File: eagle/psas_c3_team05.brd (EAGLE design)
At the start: 100 x 71.2 mm, 92 parts, among them IC1 CP2102, J1 3220-10-0100-00, U1 MIC5319 3.3V, U2 MCP73871, X1 32 MHz

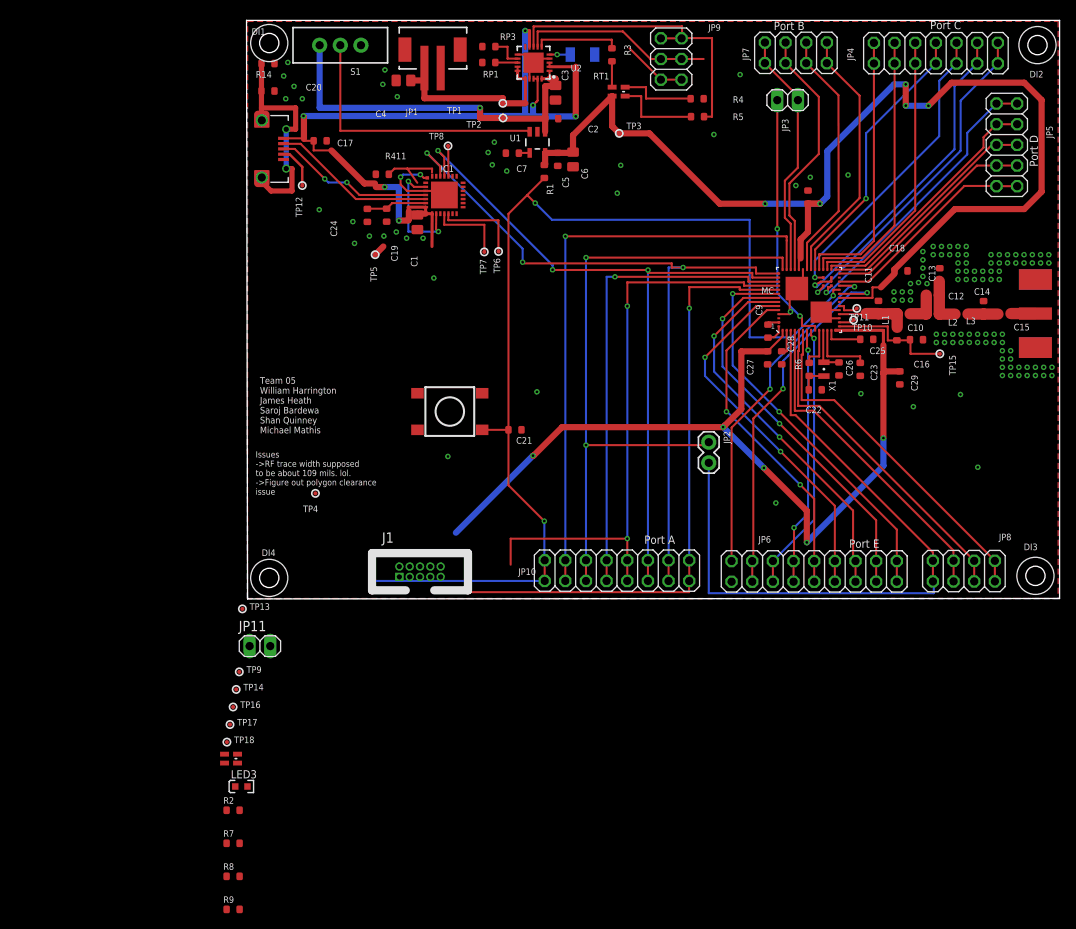
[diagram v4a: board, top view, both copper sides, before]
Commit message: major board cleanup and shrinkage. OOPS: just found out the uC pinout is wrong. Committing before doing that change.
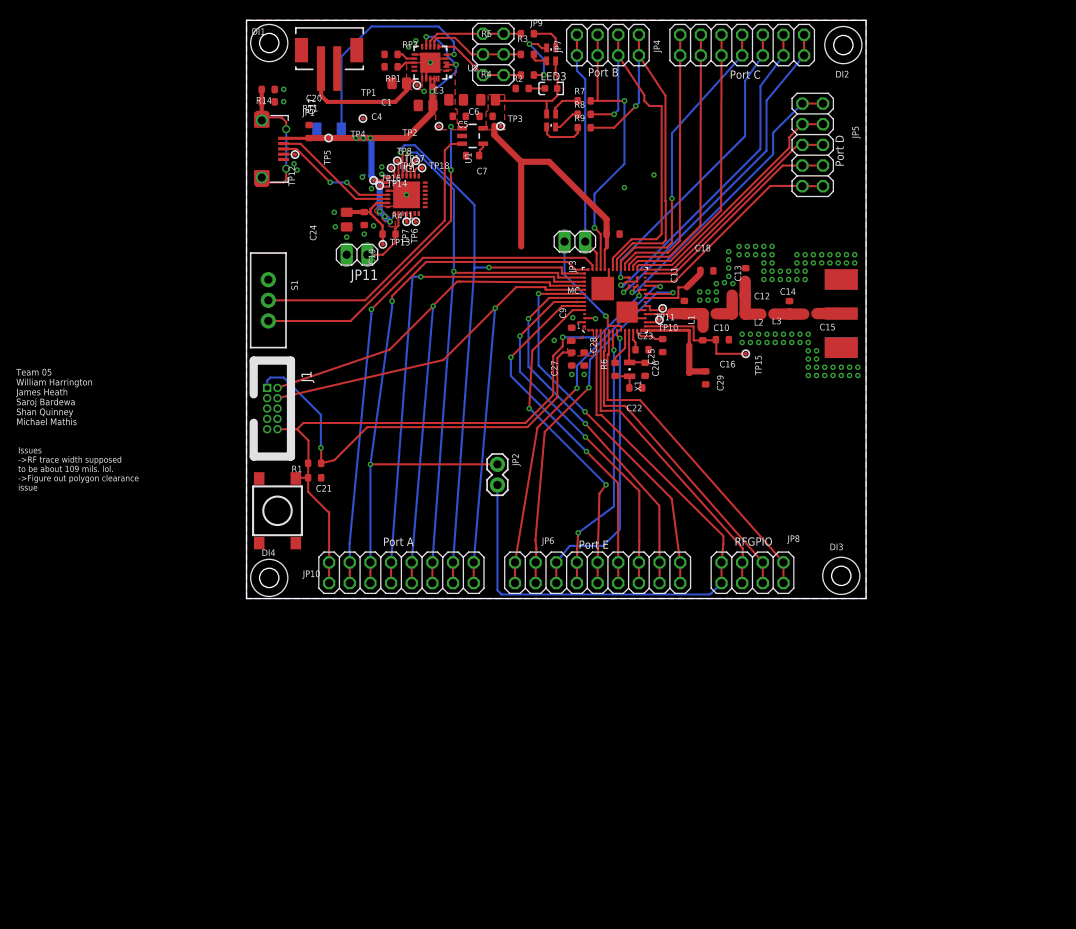
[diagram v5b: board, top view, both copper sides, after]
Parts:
- C24: device rcl_custom:.0603-B-NOSILK -> rcl_custom:.0805-B-NOSILK
- moved R9 105.4 mm to (41.5, 57.9)
- moved R8 103.2 mm to (41.5, 59.6)
- moved R7 101.0 mm to (41.5, 61.2)
- moved R2 95.6 mm to (33.9, 62.7)
- moved LED3 93.9 mm to (37.5, 62.7)
- moved LED2 87.8 mm to (37.5, 58.8), turned to 270 degrees
- moved TP18 74.6 mm to (21.6, 53.0)
- moved TP17 72.3 mm to (18.5, 53.8)
- moved TP16 67.0 mm to (15.6, 51.4)
- moved TP9 64.7 mm to (17.8, 53.0)
- moved TP14 64.4 mm to (16.4, 50.8)
- moved JP11 49.6 mm to (13.6, 42.3), turned to 180 degrees
- moved TP13 48.0 mm to (16.8, 43.6)
- moved TP4 46.5 mm to (14.3, 59.0)
- moved R1 45.7 mm to (8.38, 16.6), turned to 0 degrees
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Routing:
- net 3.3V: track 258.2 -> 127.2 mm, vias 10 -> 1
- net PTA20/!RESET: track 134.6 -> 78.7 mm, vias 3 -> 2
- net VBUS: track 101.5 -> 57.6 mm, vias 6 -> 9
- net STAT1/LBO: track 39.3 -> 12.2 mm
- net N$6: track 2.55 -> 27.7 mm
- net PTA1: track 95.0 -> 76.7 mm, vias 3 -> 2
- net RESET(RF): track 31.3 -> 14.9 mm, vias 2 -> 1
- net PTB17: track 32.1 -> 47.6 mm, vias 0 -> 1
- net N$30: track 22.8 -> 7.80 mm, vias 2 -> 0
- net PTB2: track 31.2 -> 46.2 mm, vias 0 -> 1
- net PTA2: track 91.0 -> 76.2 mm, vias 3 -> 2
- net STAT2: track 23.7 -> 12.3 mm
- net GND: track 34.0 -> 22.8 mm, vias 127 -> 114
- net SHIELD: track 28.1 -> 17.7 mm
- net N$5: track 10.8 -> 1.27 mm
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- added copper zone on layer 1, net 3.3V
- added copper zone on layer 1, net V+
- added copper zone on layer 1, net VBUS
- added copper zone on layer 1, net VOUT
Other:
- board size 100 x 71.2 mm -> 76.2 x 71.1 mm
- board text added: "RFGPIO"

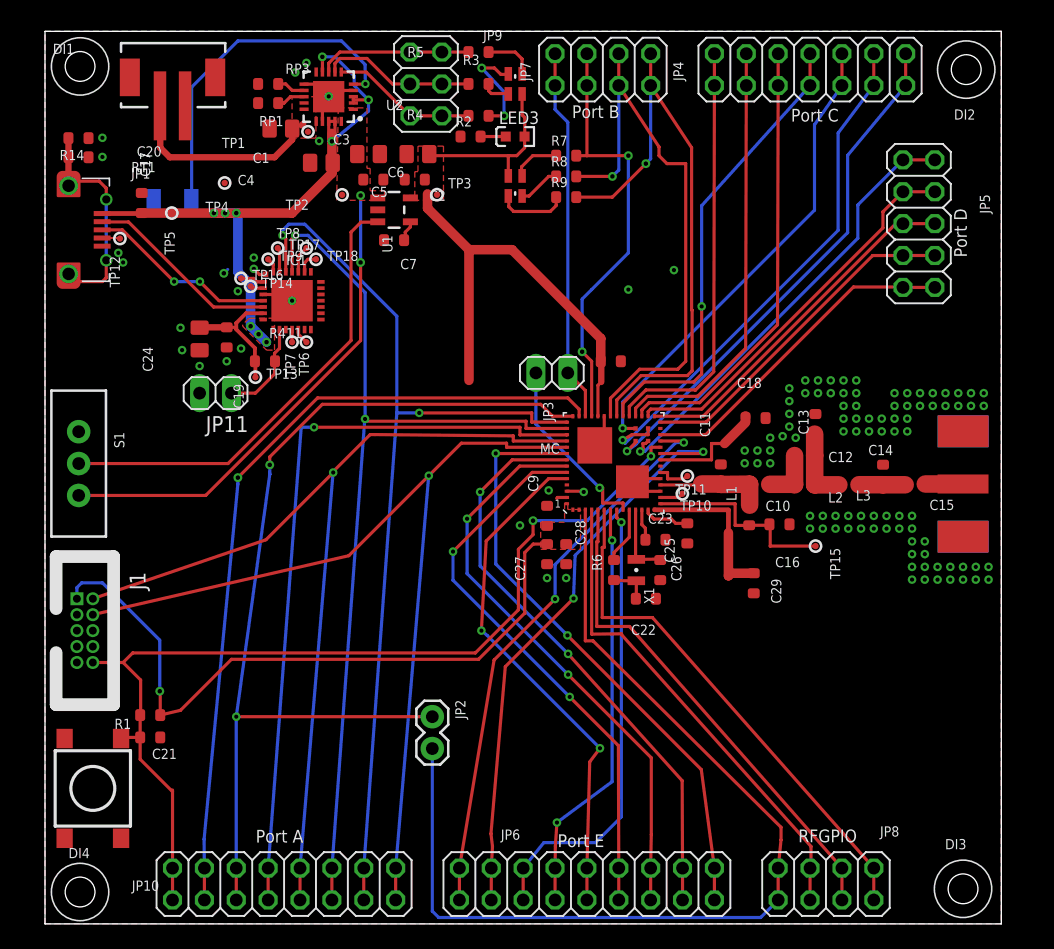
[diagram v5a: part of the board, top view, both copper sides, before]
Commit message: Well, sometimes you just have to start over :( Fixed flipped chip. No more airwires.
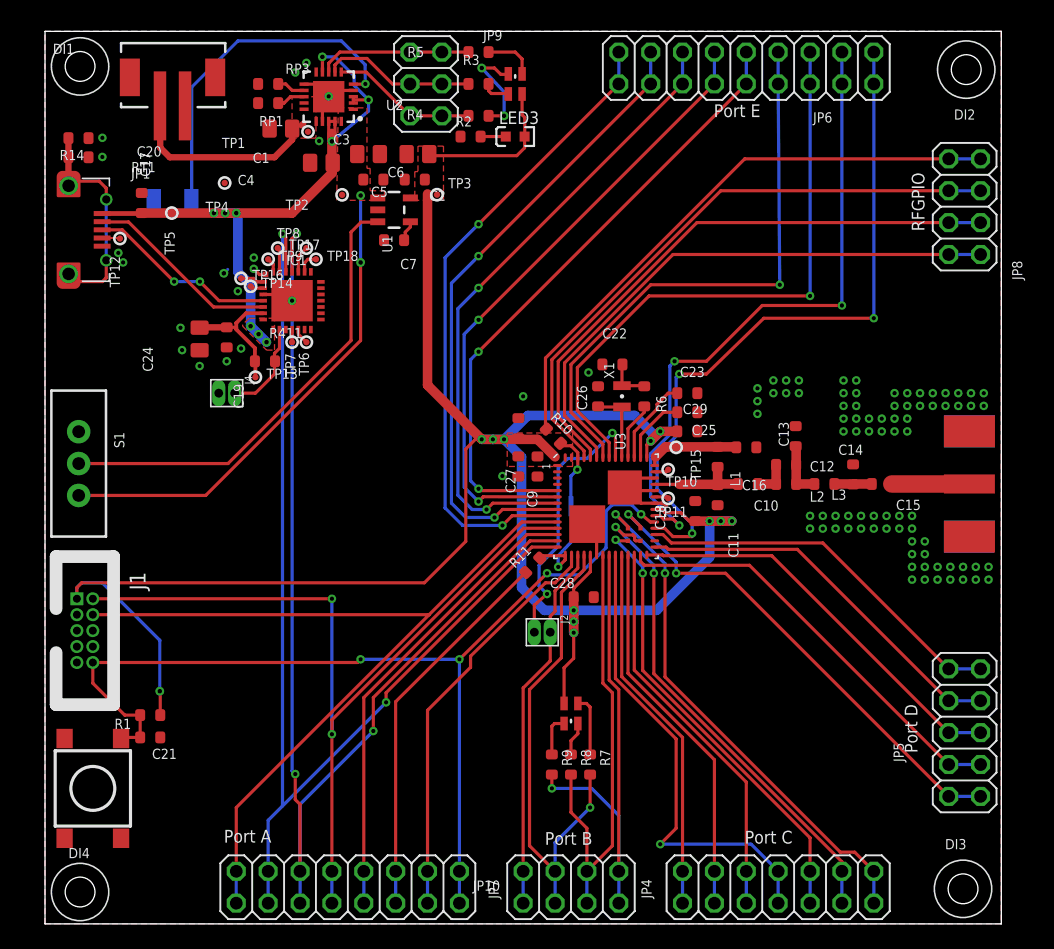
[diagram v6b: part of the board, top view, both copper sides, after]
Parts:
- removed JP11, JP3: (no value), pinhead:1X02
- removed JP2: (no value), SparkFun-v5:1X02
- removed MC: MKW01Z128, psas_c3:MKW01Z128
- added J2, J4: 1.27MM_HDR_2X12X1, headers:1.27MM_2X1
- added R10, R11: NP, rcl_custom:.0603-B-NOSILK
- added U3: MKW01Z128, psas_c3:MKW01Z128
- added W1: (no value), apdm:CONNECTION-BUTT-0.4
- moved JP6 66.3 mm to (55.9, 68.2), turned to 180 degrees
- moved JP4 65.2 mm to (58.4, 2.92)
- moved JP7 65.2 mm to (41.9, 2.92)
- moved JP8 55.1 mm to (73.3, 57.1), turned to 90 degrees
- moved R7 48.6 mm to (43.4, 12.7), turned to 270 degrees
- moved R8 46.9 mm to (41.9, 12.7), turned to 270 degrees
- moved R9 45.2 mm to (40.4, 12.7), turned to 270 degrees
- moved LED2 42.3 mm to (41.9, 16.8)
- moved JP5 40.7 mm to (73.3, 15.2), turned to 90 degrees
- moved C22 18.9 mm to (45.2, 44.6), turned to 180 degrees
- moved C26 14.7 mm to (44.1, 42.0), turned to 90 degrees
- moved R6 14.1 mm to (47.8, 42.0), turned to 270 degrees
- moved X1 13.9 mm to (46.0, 42.0), turned to 90 degrees
- moved TP15 13.6 mm to (50.3, 38.0)
- moved C29 13.2 mm to (51.2, 39.2), turned to 0 degrees
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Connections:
- removed net N$14: C25.1, MC.44
- removed net N$16: JP8.1, JP8.2, MC.51
- removed net N$20: JP8.3, JP8.4, MC.52
- removed net N$22: C23.1, MC.45
- removed net N$23: JP8.5, JP8.6, MC.53
- new net DIO2: JP8.1, JP8.2, U3.51
- new net DIO3: JP8.3, JP8.4, U3.52
- new net DIO4: JP8.5, JP8.6, U3.53
- new net DIO5-JMP: JP8.7, JP8.8, R10.1
- new net PTA18-JMP: JP10.11, JP10.12, R11.1
- new net VR_ANA: C25.1, U3.44
- new net VR_DIG: C23.1, U3.45
- net 3.3V: now also U3.1, U3.19, U3.35, U3.43, U3.55, U3.56; no longer MC.1, MC.19, MC.35, MC.43, MC.55, MC.56
- net DIO5/CLKOUT: now also R10.2, U3.54, W1.P1; no longer JP2.2, JP8.7, JP8.8, MC.54
- net GND: now also J4.2, U3.2, U3.20, U3.3, U3.36, U3.38, U3.4, U3.40, U3.PGND1, U3.PGND2; no longer JP11.2, MC.2, MC.20, MC.3, MC.36, MC.38, MC.4, MC.40, MC.PGND1, MC.PGND2
- net N$13: now also U3.41; no longer MC.41
- net N$15: now also U3.37; no longer MC.37
- net N$30: now also J4.1; no longer JP11.1
- net PTA0: now also U3.10; no longer MC.10
- net PTA1: now also U3.14; no longer MC.14
- net PTA18: now also R11.2, U3.15, W1.P2; no longer JP10.11, JP10.12, JP2.1, MC.15
- net PTA19/XTAL0: now also U3.16; no longer MC.16
- net PTA2: now also U3.13; no longer MC.13
- net PTA20/!RESET: now also U3.33; no longer MC.33
- net PTA3: now also U3.11; no longer MC.11
- net PTA4: now also U3.12; no longer MC.12
- net PTB0: now also J2.1, U3.17; no longer JP3.1, MC.17
- net PTB1: now also U3.18; no longer MC.18
- net PTB17: now also U3.22; no longer MC.22
- net PTB2: now also U3.21; no longer MC.21
- net PTC1: now also U3.24; no longer MC.24
- net PTC2: now also U3.25; no longer MC.25
- net PTC3: now also U3.26; no longer MC.26
- net PTC4: now also U3.23; no longer MC.23
- net PTC5: now also U3.59; no longer MC.59
- net PTC6: now also U3.60; no longer MC.60
- net PTC7: now also U3.57; no longer MC.57
- net PTD0: now also U3.58; no longer MC.58
- net PTD4: now also U3.27; no longer MC.27
- net PTD5: now also U3.28; no longer MC.28
- net PTD6: now also U3.29; no longer MC.29
- net PTD7: now also U3.31; no longer MC.31
- net PTE0: now also U3.32; no longer MC.32
- net PTE1: now also U3.34; no longer MC.34
- net PTE16: now also U3.5; no longer MC.5
- net PTE17: now also U3.6; no longer MC.6
- net PTE18: now also U3.7; no longer MC.7
- net PTE19: now also U3.8; no longer MC.8
- net PTE2: now also U3.49; no longer MC.49
- net PTE3: now also U3.50; no longer MC.50
- net PTE30: now also U3.9; no longer MC.9
- net RESET(RF): now also J2.2, U3.48; no longer JP3.2, MC.48
- net RFIO: now also U3.39; no longer MC.39
- net VR_PA: now also U3.42; no longer MC.42
- net XTA: now also U3.46; no longer MC.47
- net XTB: now also U3.47; no longer MC.46
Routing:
- net DIO5/CLKOUT: track 79.3 -> 5.79 mm, vias 0 -> 1
- net PTA18: track 77.5 -> 8.14 mm, vias 2 -> 1
- net DIO4: track 0.00 -> 48.6 mm
- net DIO5-JMP: track 0.00 -> 47.0 mm
- net DIO3: track 0.00 -> 47.0 mm
- net 3.3V: track 127.2 -> 173.8 mm, vias 1 -> 12
- net DIO2: track 0.00 -> 45.3 mm
- net N$16: track 41.9 -> 0.00 mm
- net N$20: track 40.2 -> 0.00 mm
- net N$23: track 39.3 -> 0.00 mm
- net PTA19/XTAL0: track 64.5 -> 33.0 mm, vias 1 -> 0
- net PTA18-JMP: track 0.00 -> 30.7 mm
- net PTA4: track 59.6 -> 37.2 mm, vias 1 -> 0
- net PTA2: track 76.2 -> 93.1 mm, vias 2 -> 3
- net PTE3: track 33.4 -> 46.3 mm, vias 2 -> 1
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
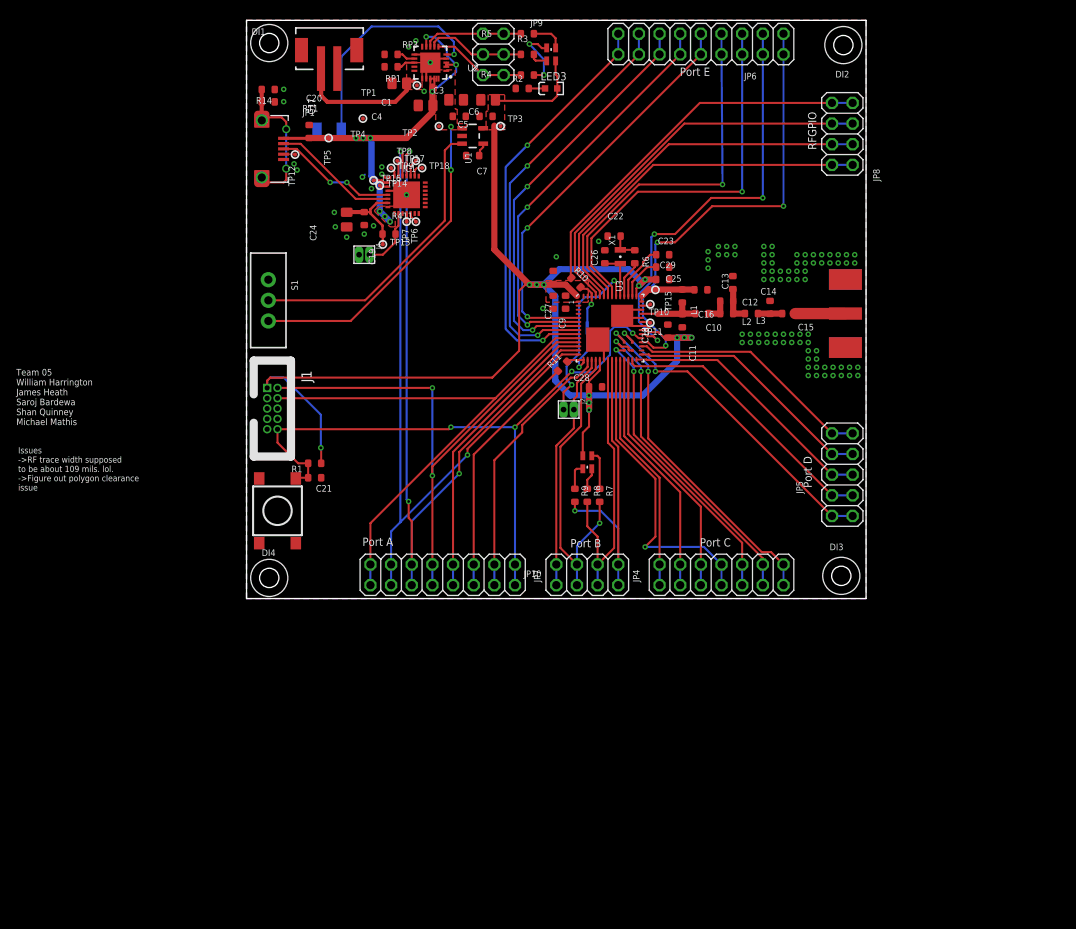
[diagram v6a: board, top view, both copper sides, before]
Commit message: Vias. Lots and lots of ground vias. Stitched until my dogs threw up. Checked ERCs and DRCs, fixed things. Forgot to say added jumper and NP zero ohms for 32 MHz clock line -- running that away from the chip is nutso crazy. Resized TNAMES and placed. Still more to do, emailing to Will.
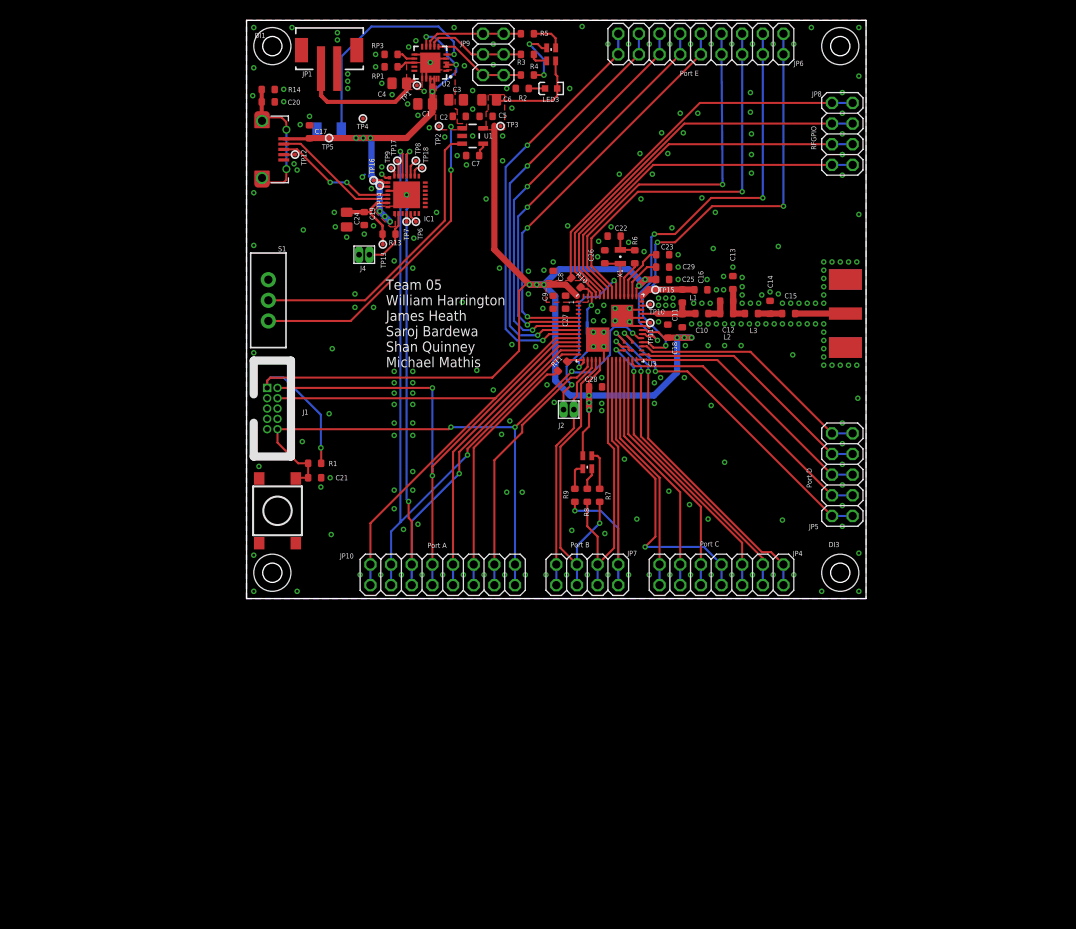
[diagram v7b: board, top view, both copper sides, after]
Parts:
- moved DI4 0.74 mm to (3.17, 3.17)
- moved DI1 0.54 mm to (3.17, 67.9)
- moved DI2 0.40 mm to (73.0, 67.9)
- moved DI3 0.40 mm to (73.0, 3.17)
- moved C1 0.19 mm to (22.0, 60.8)
- moved C6 0.13 mm to (29.8, 61.3)
- moved CF1 0.06 mm to (1.91, 55.2)
- moved TP5 0.06 mm to (10.2, 56.6)
- moved C17 0.05 mm to (7.75, 57.4)
- renumbered R411 to R13
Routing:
- net PTA2: track 93.1 -> 93.9 mm
- net 3.3V: track 173.8 -> 174.6 mm
- net GND: track 22.2 -> 21.4 mm, vias 100 -> 287
- net PTA18-JMP: track 30.7 -> 31.2 mm
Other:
- board text removed: "Issues ->RF trace width supposed to be about 109 mils. lol. ->Figure out polygon clearance issue"
